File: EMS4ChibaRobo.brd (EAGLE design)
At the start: 51 x 51.5 mm, 31 parts, among them CON1 XT60PB-F, CON2 XT60PB-M, CON3 XT60PB-M, Q2 BUZ11BH, U1 V23134J1052D642, U10 MC34063AD, U4 TLP184, U9 XC6206

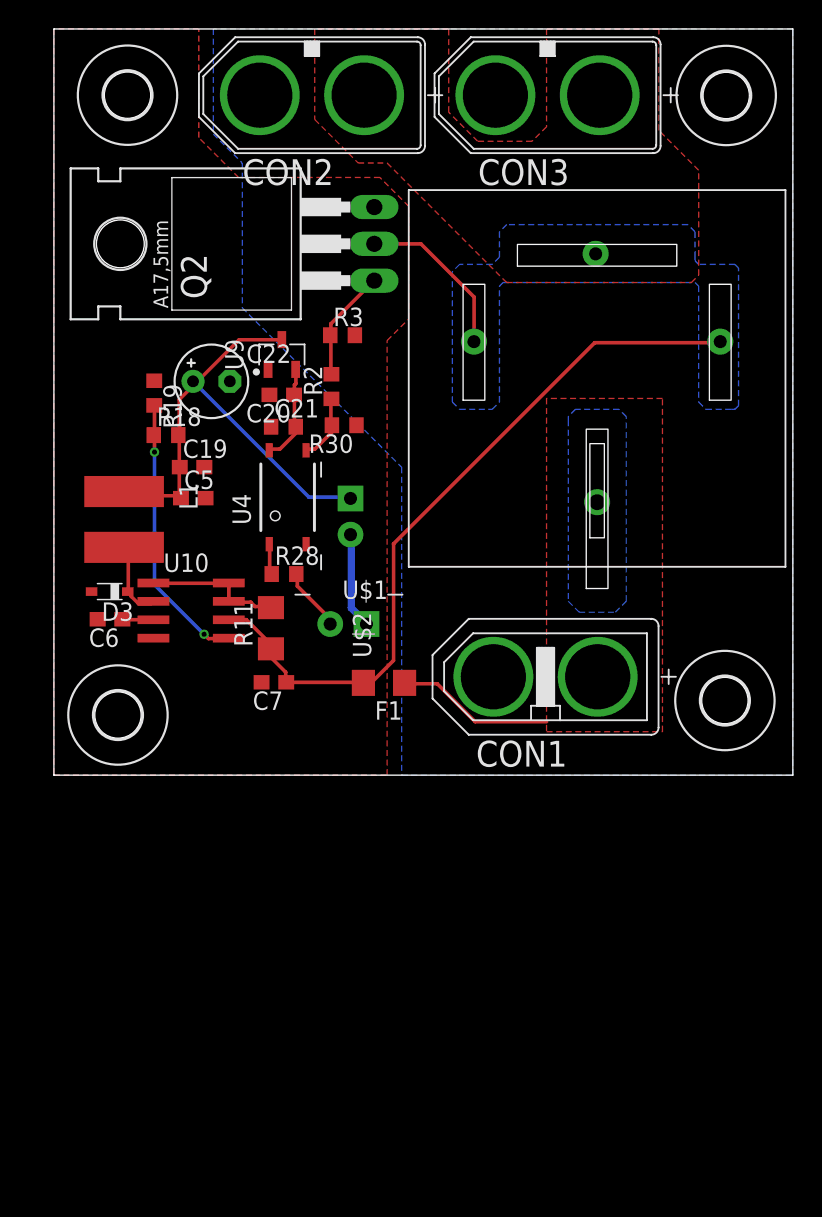
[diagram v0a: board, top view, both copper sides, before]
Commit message: ねじ穴を修正
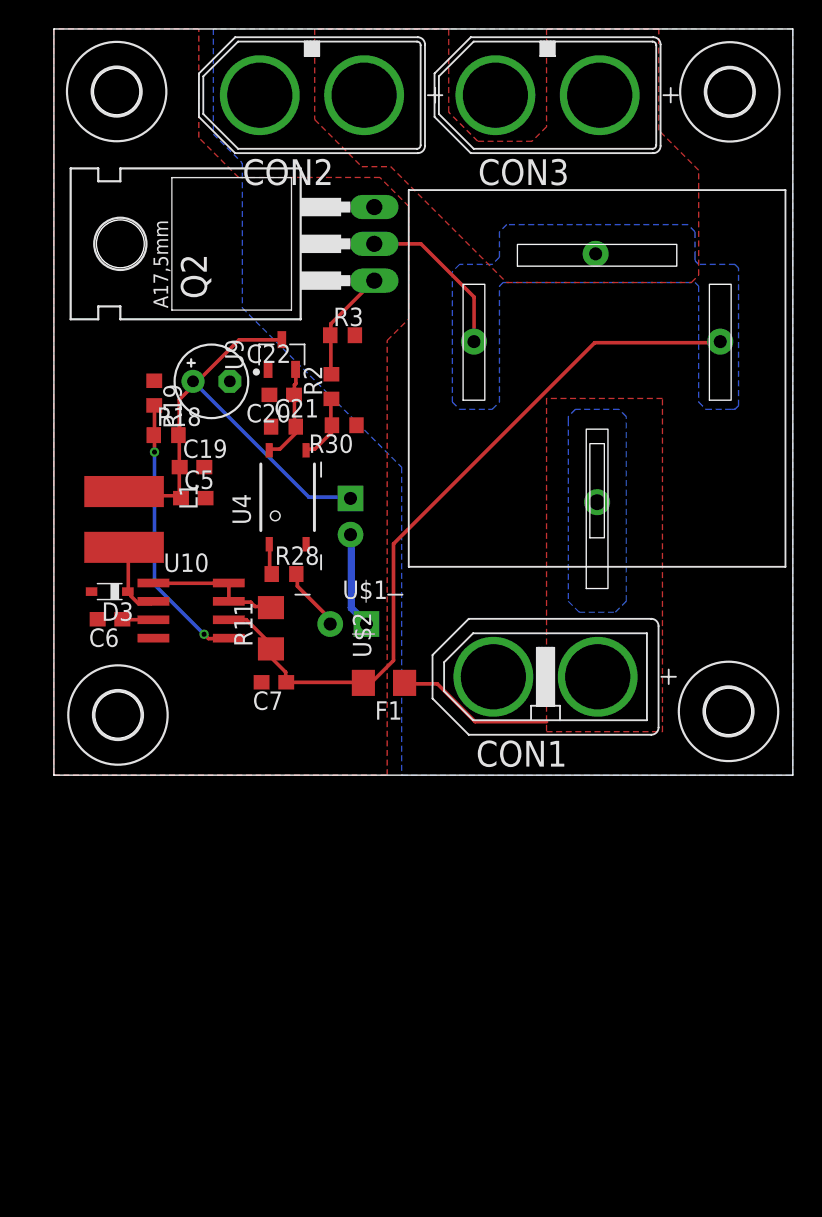
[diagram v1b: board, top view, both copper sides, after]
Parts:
- moved H1 0.79 mm to (4.33, 75.2)
- moved H3 0.79 mm to (46.6, 32.4)
- moved H2 0.35 mm to (46.6, 75.2)
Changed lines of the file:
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@@
 <drawing>
 <settings>
-<setting alwaysvectorfont="yes"/>
+<setting alwaysvectorfont="no"/>
 <setting verticaltext="up"/>
 </settings>
@@
 <attribute name="VALUE" x="24.05" y="36.91" size="1.27" layer="27" rot="R180"/>
 </element>
-<element name="H1" library="holes" library_urn="urn:adsk.eagle:library:237" package="3,2" package3d_urn="urn:adsk.eagle:package:14275/1" value="MOUNT-HOLE3.2" x="5.08" y="74.93" smashed="yes">
-<attribute name="POPULARITY" value="7" x="46.99" y="-13.97" size="1.778" layer="27" display="off"/>
-</element>
-<element name="H2" library="holes" library_urn="urn:adsk.eagle:library:237" package="3,2" package3d_urn="urn:adsk.eagle:package:14275/1" value="MOUNT-HOLE3.2" x="46.4" y="74.91" smashed="yes">
-<attribute name="POPULARITY" value="7" x="97.2" y="-13.99" size="1.778" layer="27" display="off"/>
-</element>
-<element name="H3" library="holes" library_urn="urn:adsk.eagle:library:237" package="3,2" package3d_urn="urn:adsk.eagle:package:14275/1" value="MOUNT-HOLE3.2" x="46.31" y="33.15" smashed="yes">
-<attribute name="POPULARITY" value="7" x="106" y="-55.75" size="1.778" layer="27" display="off"/>
+<element name="H1" library="holes" library_urn="urn:adsk.eagle:library:237" package="3,2" package3d_urn="urn:adsk.eagle:package:14275/1" value="MOUNT-HOLE3.2" x="4.33" y="75.18" smashed="yes">
+<attribute name="POPULARITY" value="7" x="46.24" y="-13.72" size="1.778" layer="27" display="off"/>
+</element>
+<element name="H2" library="holes" library_urn="urn:adsk.eagle:library:237" package="3,2" package3d_urn="urn:adsk.eagle:package:14275/1" value="MOUNT-HOLE3.2" x="46.65" y="75.16" smashed="yes">
+<attribute name="POPULARITY" value="7" x="97.45" y="-13.74" size="1.778" layer="27" display="off"/>
+</element>
+<element name="H3" library="holes" library_urn="urn:adsk.eagle:library:237" package="3,2" package3d_urn="urn:adsk.eagle:package:14275/1" value="MOUNT-HOLE3.2" x="46.56" y="32.4" smashed="yes">
+<attribute name="POPULARITY" value="7" x="106.25" y="-56.5" size="1.778" layer="27" display="off"/>
 </element>
 <element name="H4" library="holes" library_urn="urn:adsk.eagle:library:237" package="3,2" package3d_urn="urn:adsk.eagle:package:14275/1" value="MOUNT-HOLE3.2" x="4.42" y="32.15" smashed="yes">
@@
 <contactref element="CON2" pad="-"/>
 <contactref element="CON3" pad="-"/>
-<wire x1="30.3812" y1="74.8464" x2="30.47" y2="74.93" width="0.25" layer="16"/>
 <polygon width="0.25" layer="16" thermals="no">
 <vertex x="24" y="28"/>
@@
 <vertex x="18" y="79.5"/>
 <vertex x="18" y="73.25"/>
-<vertex x="21" y="70.25"/>
-<vertex x="23" y="70.25"/>
+<vertex x="21.25" y="70"/>
+<vertex x="23.25" y="70"/>
 </polygon>
 </signal>

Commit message: 微調整
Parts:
- moved U9 0.25 mm to (15.5, 57.0)
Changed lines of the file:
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@@
 <attribute name="VALUE" x="19.94" y="45.275" size="1.27" layer="27" rot="R90"/>
 </element>
-<element name="U9" library="torex" package="SOT95P240X110-3" package3d_urn="urn:adsk.eagle:package:6993131/1" value="XC6206" x="15.73" y="57.03" smashed="yes" rot="R90">
-<attribute name="NAME" x="13.0864" y="57.03" size="1.27" layer="25" rot="R90" align="bottom-center"/>
-<attribute name="VALUE" x="17.9336" y="57.03" size="1.27" layer="27" rot="R90" align="top-center"/>
+<element name="U9" library="torex" package="SOT95P240X110-3" package3d_urn="urn:adsk.eagle:package:6993131/1" value="XC6206" x="15.48" y="57.03" smashed="yes" rot="R90">
+<attribute name="NAME" x="12.8364" y="57.03" size="1.27" layer="25" rot="R90" align="bottom-center"/>
+<attribute name="VALUE" x="17.6836" y="57.03" size="1.27" layer="27" rot="R90" align="top-center"/>
 </element>
 <element name="C19" library="rcl" library_urn="urn:adsk.eagle:library:334" package="C0603" package3d_urn="urn:adsk.eagle:package:23616/2" value="1u" x="9.53" y="49.26" smashed="yes">
@@
 <contactref element="U9" pad="2"/>
 <contactref element="C20" pad="1"/>
-<wire x1="16.599" y1="54.9276" x2="16.599" y2="54.324" width="0.25" layer="1"/>
-<wire x1="16.6996" y1="55.0282" x2="16.599" y2="54.9276" width="0.25" layer="1"/>
-<wire x1="16.6996" y1="55.9336" x2="16.6996" y2="55.0282" width="0.25" layer="1"/>
-<wire x1="16.599" y1="54.324" x2="16.57" y2="54.25" width="0.25" layer="1"/>
-<wire x1="16.6996" y1="55.9336" x2="16.68" y2="56.0055" width="0.25" layer="1"/>
 <wire x1="15.593" y1="50.5012" x2="14.8888" y2="50.5012" width="0.25" layer="1"/>
 <wire x1="16.6996" y1="51.6078" x2="15.593" y2="50.5012" width="0.25" layer="1"/>
@@
 <wire x1="16.599" y1="54.2234" x2="16.57" y2="54.25" width="0.25" layer="1"/>
 <wire x1="16.599" y1="52.1108" x2="16.69" y2="52.05" width="0.25" layer="1"/>
+<wire x1="16.57" y1="54.25" x2="16.57" y2="55.8655" width="0.25" layer="1"/>
+<wire x1="16.57" y1="55.8655" x2="16.43" y2="56.0055" width="0.25" layer="1"/>
 </signal>
 <signal name="N$30">
@@
 <wire x1="8.551" y1="47.282" x2="8.77" y2="47.12" width="0.25" layer="1"/>
 <wire x1="4.9294" y1="47.4832" x2="4.84" y2="47.575" width="0.25" layer="1"/>
-<wire x1="12.7762" y1="58.0462" x2="15.6936" y2="58.0462" width="0.25" layer="1"/>
+<wire x1="12.7762" y1="58.0462" x2="15.4436" y2="58.0462" width="0.25" layer="1"/>
 <wire x1="9.9594" y1="55.2294" x2="12.7762" y2="58.0462" width="0.25" layer="1"/>
 <wire x1="9.6576" y1="55.2294" x2="9.9594" y2="55.2294" width="0.25" layer="1"/>
-<wire x1="15.6936" y1="58.0462" x2="15.73" y2="58.0545" width="0.25" layer="1"/>
+<wire x1="15.4436" y1="58.0462" x2="15.48" y2="58.0545" width="0.25" layer="1"/>
 <wire x1="9.6576" y1="55.2294" x2="9.6" y2="55.18" width="0.25" layer="1"/>
 <wire x1="17.605" y1="47.1814" x2="20.4218" y2="47.1814" width="0.25" layer="16"/>

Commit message: 大幅な設計変更
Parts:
- removed C22: 47u, rcl:E2,5-5
- removed C5, C7: 100n, rcl:C0603
- removed C6: 100p, rcl:C0603
- removed D3: PMEG6010CEJ,115, nexperia:SOD323_ST
- removed L1: L5852, inductors:L5852
- removed Q2: BUZ11BH, transistor-power:TO220BH
- removed R11: 0.68, rcl:R1206
- removed R18: 3.6k, rcl:R0603
- removed R19: 1.2k, rcl:R0603
- removed R28, R30: 1k, rcl:R0603
- removed U10: MC34063AD, mc34063:SOIC8
- removed U4: TLP184, md201x:11-4M1S
- added C1: 22u, rcl:E2,5-5
- added C2: 100n, rcl:C0603
- added IC1: 7805DT, linear:TO252
- added Q1: BUZ11BH, transistor-power:TO220BH
- added U$3, U$4: XH-2-STRAIGHT, con-xh:CON-XH-2-STRAIGHT
- moved R3 42.0 mm to (13.6, 16.8), turned to 270 degrees
- moved C20 36.7 mm to (6.50, 18.7), turned to 270 degrees
- moved U9 36.6 mm to (10.5, 20.8), turned to 0 degrees
- moved C21 35.6 mm to (3.70, 18.6), turned to 90 degrees
- moved C19 33.5 mm to (10.7, 15.7), turned to 180 degrees
- moved R2 32.0 mm to (11.1, 23.9), turned to 0 degrees
- moved CON2 28.0 mm to (17.8, 46.9)
- moved CON3 28.0 mm to (34.1, 46.9)
- moved H1 28.0 mm to (4.33, 47.2)
- moved U1 28.0 mm to (37.5, 27.4)
- moved CON1 28.0 mm to (33.9, 6.79)
- moved H2 28.0 mm to (46.6, 47.2)
- moved H3 28.0 mm to (46.6, 4.40)
- moved H4 28.0 mm to (4.42, 4.15)
- moved U$1 26.6 mm to (4.64, 24.0), turned to 0 degrees
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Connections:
- removed net N$1: R11.2, U10.1, U10.7, U10.8
- removed net N$26: D3.C, L1.P$1, U10.2
- removed net N$27: C6.1, U10.3
- removed net N$28: R18.1, R19.2, U10.5
- removed net N$30: R28.1, U4.1
- removed net SEND_EMS: U$1.P$2, U$2.P$1
- new net LOG_OUT: F1.1, U$3.P$2, U$4.P$2
- net !EMS: now also U$1.P$1; no longer R30.2, U4.3
- net !EMS_ISO: no longer R28.2
- net +12V: now also C1.+, IC1.1; no longer C7.1, R11.1, U10.6
- net +3V3: now also U$1.P$2; no longer U4.4
- net +5V: now also C2.1, IC1.2; no longer C22.+, C5.1, L1.P$2, R18.2, U$1.P$1
- net BATT_POWER: no longer F1.1
- net GNDIO: now also C1.-, C2.2, IC1.3, Q1.S, U$2.P$1, U$3.P$1, U$4.P$1; no longer C22.-, C5.2, C6.2, C7.2, D3.A, Q2.S, R19.1, R30.1, U10.4, U4.2
- net N$6: now also Q1.D; no longer Q2.D
- net N$7: now also Q1.G; no longer Q2.G
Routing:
- net +5V: track 34.0 -> 6.79 mm
- net N$28: track 19.1 -> 0.00 mm, vias 2 -> 0
- net BATT_POWER: track 10.9 -> 0.00 mm
- net N$1: track 9.72 -> 0.00 mm
- net LOG_OUT: track 0.00 -> 8.72 mm
- net SEND_EMS: track 6.62 -> 0.00 mm
- net +12V: track 51.1 -> 45.3 mm
- net N$26: track 5.44 -> 0.00 mm
- net N$6: track 11.5 -> 16.6 mm
- net !EMS_ISO: track 4.43 -> 0.00 mm
- net !EMS: track 4.71 -> 8.89 mm
- net +3V3: track 6.87 -> 10.2 mm
- net N$27: track 2.17 -> 0.00 mm
- net N$30: track 2.12 -> 0.00 mm
- net N$7: track 7.76 -> 9.30 mm
- added copper zone on layer 16, net GNDIO

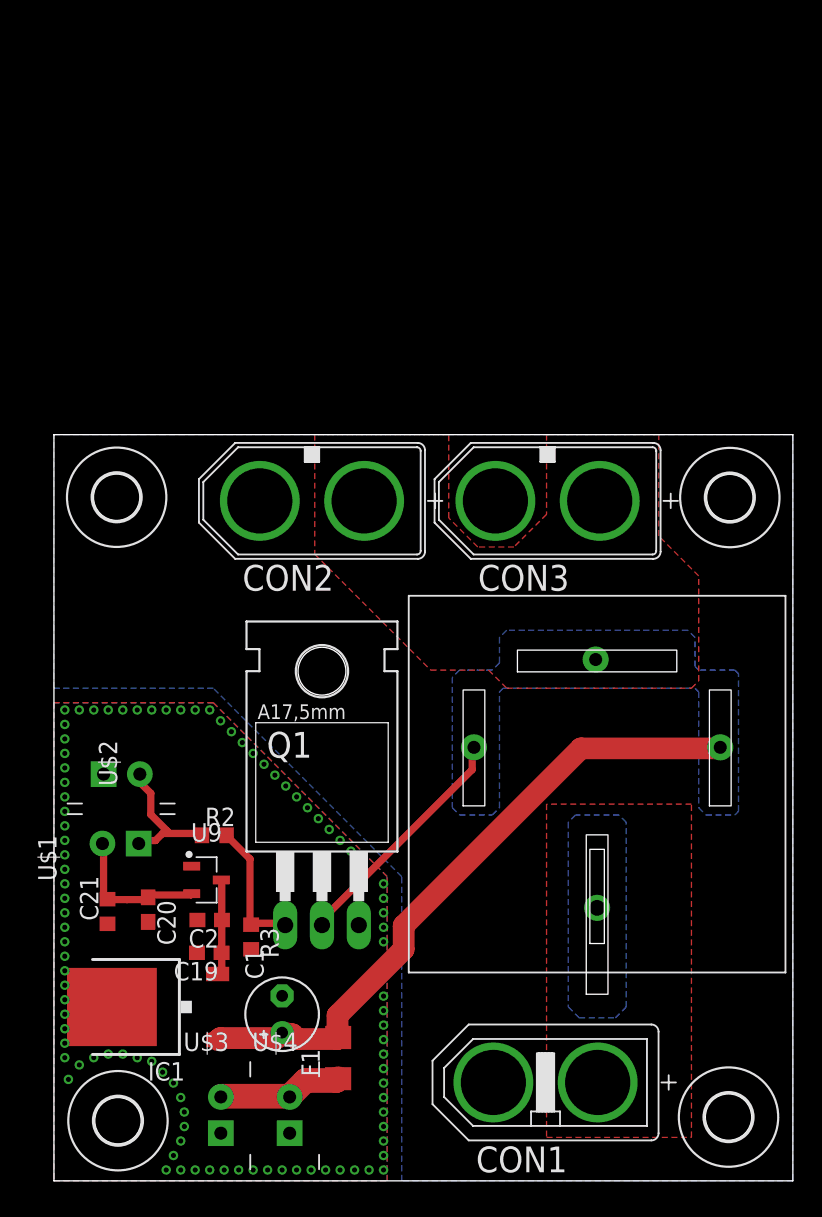
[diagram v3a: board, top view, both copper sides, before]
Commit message: relayのフットプリントの改善
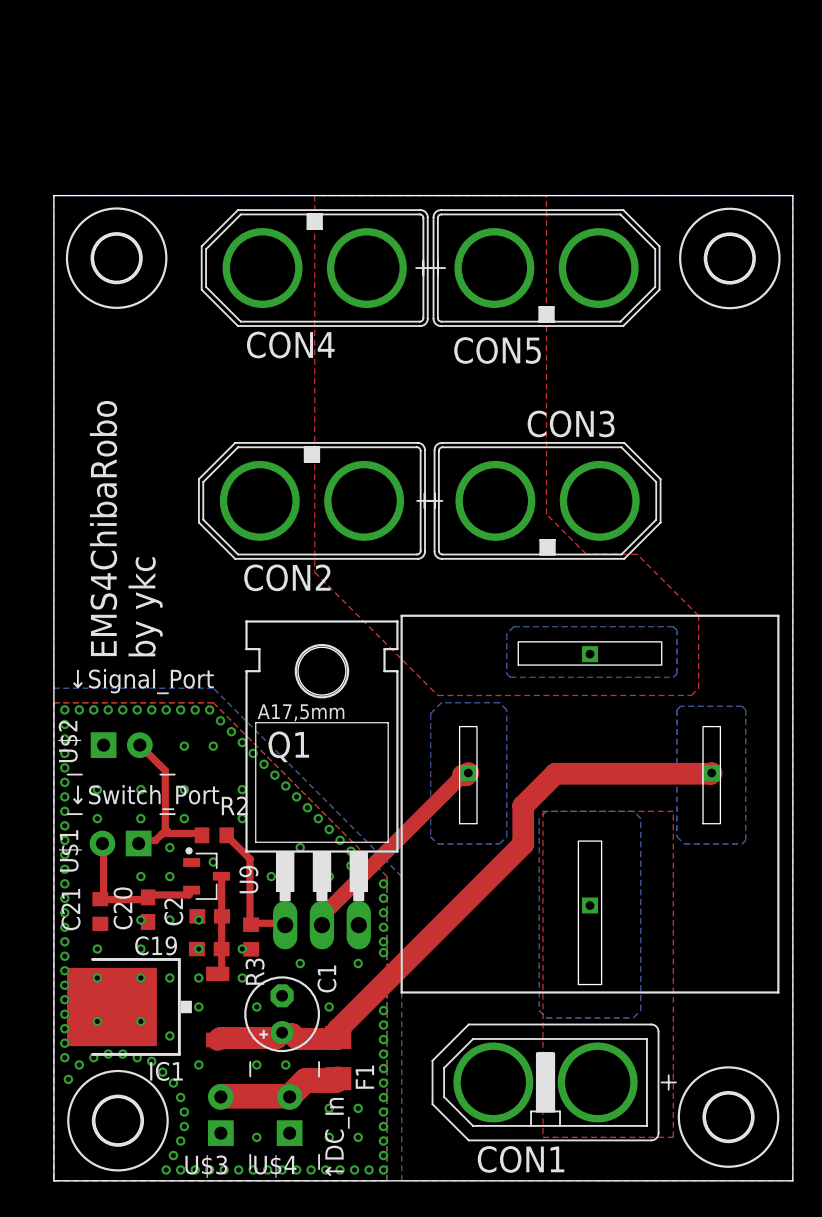
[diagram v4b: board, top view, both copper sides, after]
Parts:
- removed U1: V23134J1052D642, relay:V23134J1052D642
- added CON4, CON5: XT60PB-M, amass:XT60PB-M
- added S1: 897-1AH-C-001, relay:897-1AH-C-001
- moved H1 16.5 mm to (4.33, 63.7)
- moved H2 16.5 mm to (46.6, 63.7)
- moved U$2 2.00 mm to (4.64, 29.3)
- moved C21 0.50 mm to (3.20, 18.6)
- moved C19 0.25 mm to (10.7, 16.0)
- moved C2 0.25 mm to (10.8, 18.2)
- moved U9 0.25 mm to (10.5, 21.0)
- turned CON3 to 180 degrees
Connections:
- removed net !EMS_ISO: U$2.P$2
- removed net N$6: Q1.D, U1.1
- new net N$1: Q1.D, S1.P$3
- net !EMS: now also U$2.P$2
- net +12V: now also S1.P$2; no longer U1.2
- net BATT_POWER: now also S1.P$1; no longer U1.4
- net GND2: now also CON4.-, CON5.-
- net OUT_POWER_A: now also CON4.+, CON5.+, S1.P$4; no longer U1.3
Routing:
- net N$6: track 16.6 -> 0.00 mm
- net N$1: track 0.00 -> 14.8 mm
- net !EMS: track 8.89 -> 11.6 mm
- net +12V: track 45.3 -> 44.0 mm
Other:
- board size 51 x 51.5 mm -> 51 x 68 mm
- board text added: "EMS4ChibaRobo by ykc"
- board text added: "↑DC_In"
- board text added: "↓Signal_Port"
- board text added: "↓Switch_Port"
